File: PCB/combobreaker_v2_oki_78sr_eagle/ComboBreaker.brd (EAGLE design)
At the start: 52 x 44.5 mm, 9 parts, among them J1 7-35v

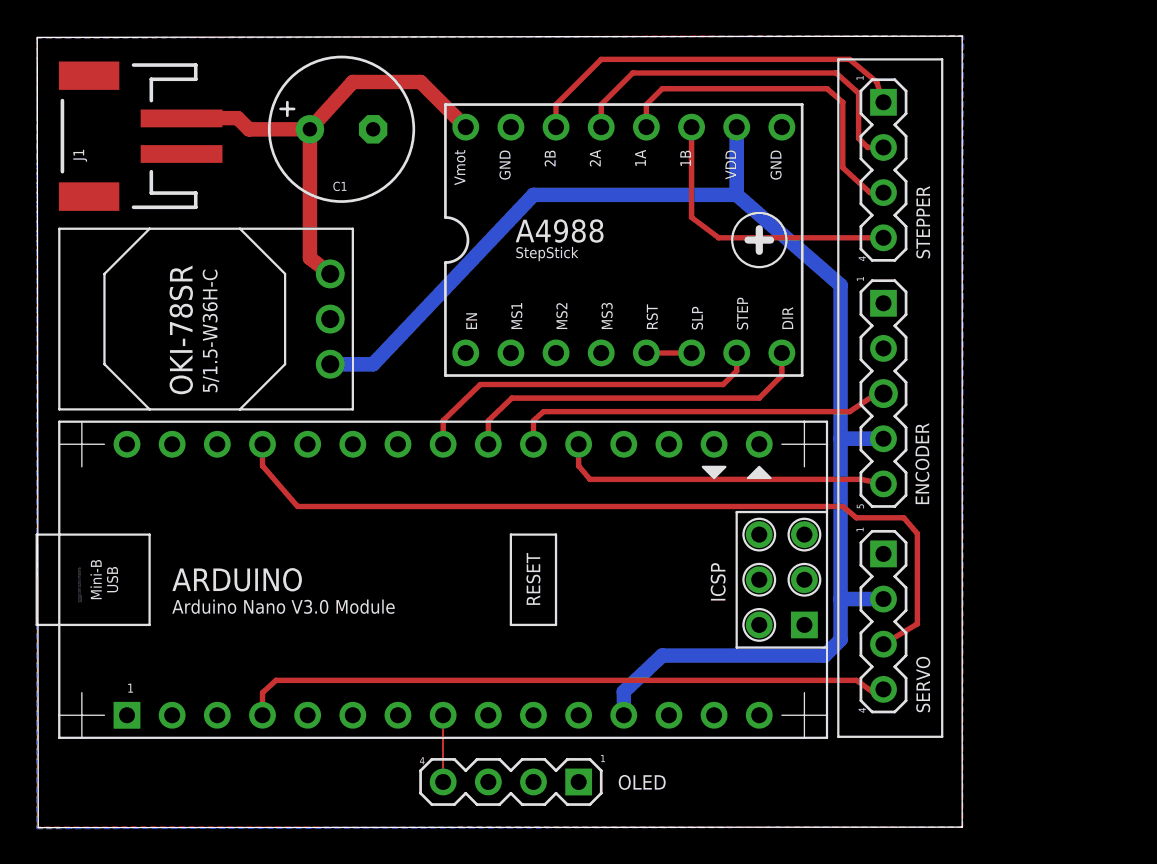
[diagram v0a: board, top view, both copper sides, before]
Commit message: Added I2C OLED Display
* Added I2C header pins for OLED display
* Reoriented JST power connector
* Rerouted VCC
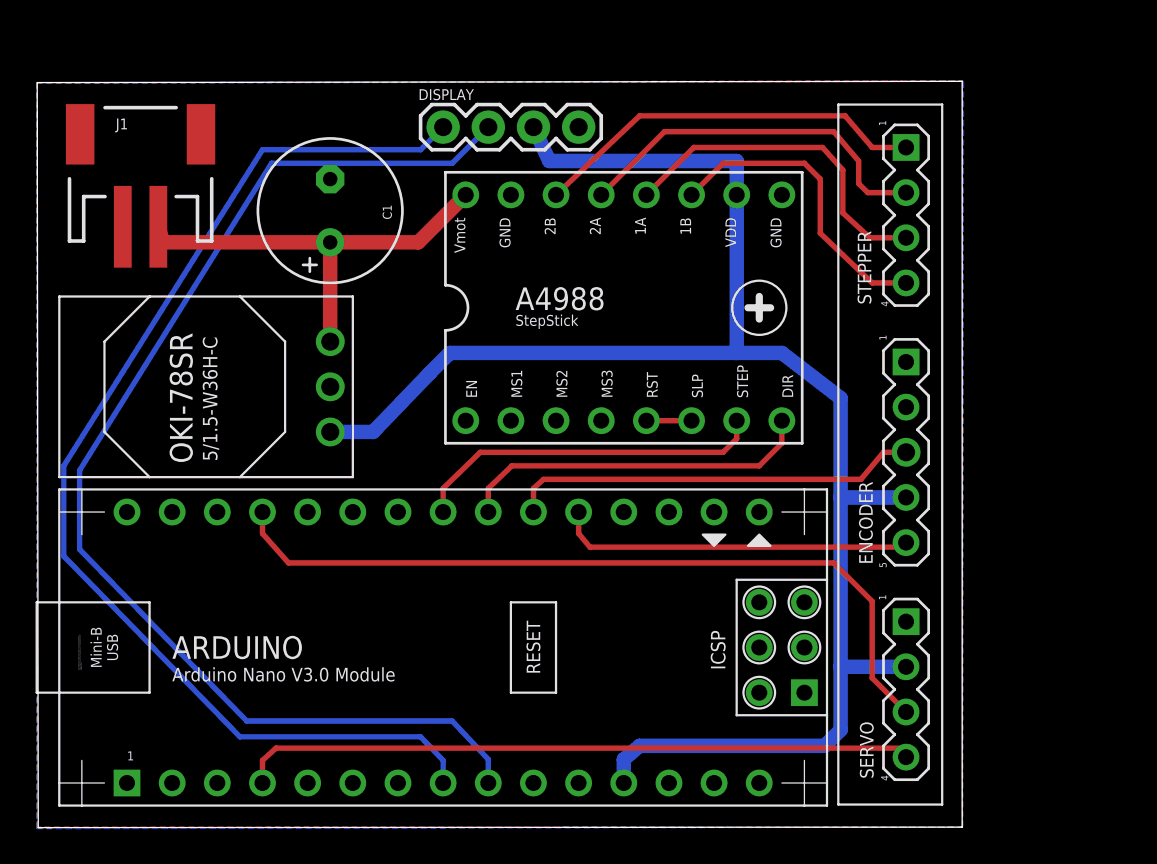
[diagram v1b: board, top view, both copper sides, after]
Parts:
- removed OLED: (no value), con-lstb:MA04-1
- added DISPLAY: OLED_I2C, SparkFun-Connectors:1X04
- moved C1 4.62 mm to (16.5, 34.7), turned to 90 degrees
- moved SERVO 4.02 mm to (48.9, 7.75)
- moved A4988 3.81 mm to (34.3, 29.2)
- moved ARDUINO 3.81 mm to (19.0, 10.1)
- moved OKI-78SR 3.81 mm to (6.35, 24.8)
- moved ENCODER 3.54 mm to (48.9, 21.1)
- moved STEPPER 2.84 mm to (48.9, 34.4)
- moved J1 1.98 mm to (5.84, 37.5), turned to 0 degrees
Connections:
- removed net N$4: OLED.2
- net +5V: now also DISPLAY.2
- net GND: now also DISPLAY.1; no longer OLED.1
- net SCL: now also DISPLAY.3; no longer OLED.3
- net SDA: now also DISPLAY.4; no longer OLED.4
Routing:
- net SCL: track 0.00 -> 67.2 mm
- net SDA: track 11.3 -> 64.2 mm
- net +5V: track 78.0 -> 95.1 mm
- net D9_SERVO: track 47.0 -> 44.2 mm
- net VCC: track 27.2 -> 24.6 mm
- net D3_CH_B_BROWN: track 21.5 -> 23.2 mm
- net D2_CH_A_WHITE: track 18.7 -> 20.2 mm
- net FEEDBACK: track 36.7 -> 38.0 mm
- net 1A_BLK: track 16.3 -> 17.3 mm
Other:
- board size 52 x 44.5 mm -> 52 x 42 mm

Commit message: Updated v2 Eagle PCB layout
* Added standoff holes
* Added descriptions
* Added mitre to board corners
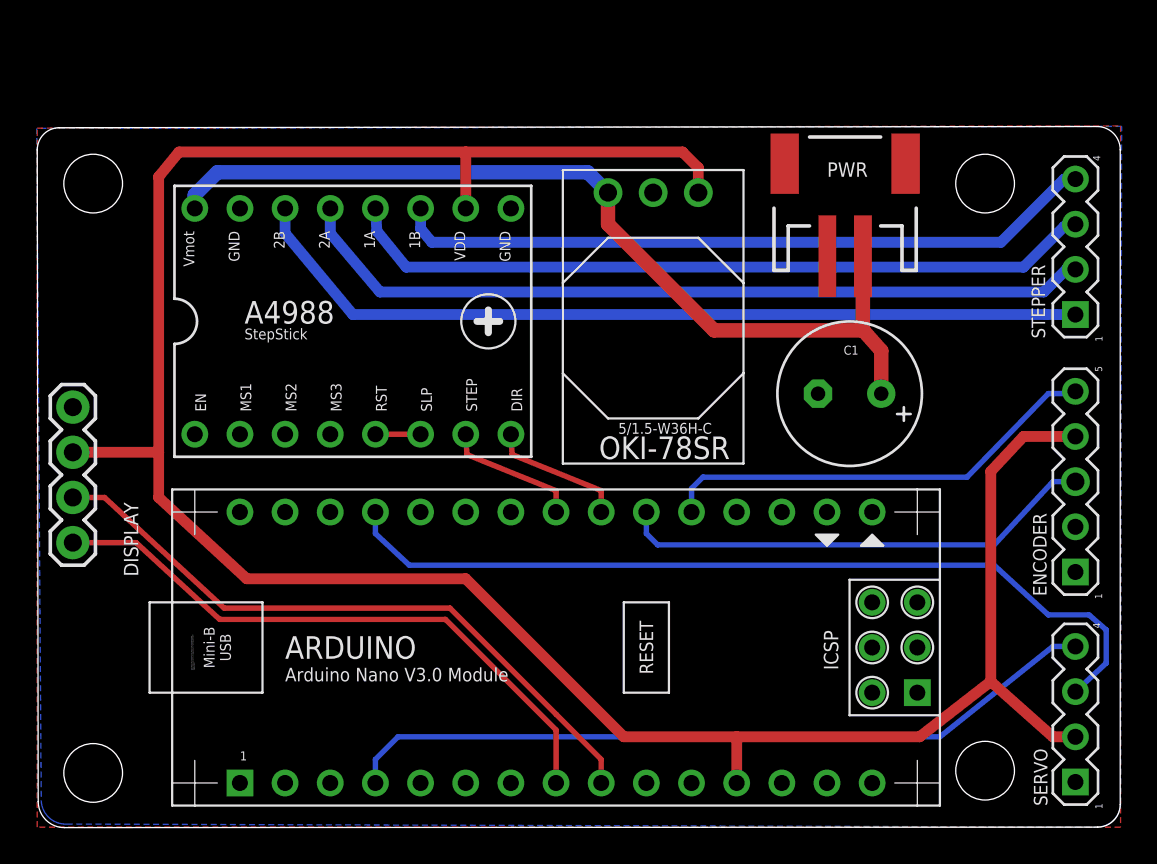
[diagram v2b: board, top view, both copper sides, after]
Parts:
- removed J1: 7-35v, SparkFun-Connectors:JST-2-SMD
- added PWR: 7-35v, SparkFun-Connectors:JST-2-SMD
- added U$1, U$2, U$3, U$4: (no value), SparkFun-Hardware:STAND-OFF
- DISPLAY: value OLED_I2C -> I2C
- moved DISPLAY 32.5 mm to (2.03, 23.6), turned to 270 degrees
- moved C1 31.0 mm to (45.7, 24.4), turned to 180 degrees
- moved OKI-78SR 28.3 mm to (34.7, 25.5), turned to 180 degrees
- moved A4988 15.3 mm to (19.1, 28.4)
- moved STEPPER 9.69 mm to (58.4, 32.6), turned to 90 degrees
- moved ENCODER 9.67 mm to (58.4, 19.4), turned to 90 degrees
- moved SERVO 9.63 mm to (58.4, 6.35), turned to 90 degrees
- moved ARDUINO 6.35 mm to (25.4, 10.1)
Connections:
- net GND: now also PWR.1; no longer J1.1
- net VCC: now also PWR.2; no longer J1.2
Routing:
- net +5V: track 95.1 -> 138.3 mm
- net SCL: track 67.2 -> 37.0 mm
- net SDA: track 64.2 -> 34.4 mm
- net VCC: track 24.6 -> 51.7 mm
- net 2B_BLU: track 22.3 -> 48.0 mm
- net 2A_RED: track 20.9 -> 45.4 mm
- net 1B_GRN: track 19.2 -> 42.5 mm
- net 1A_BLK: track 17.3 -> 39.8 mm
- net N$2: track 20.2 -> 7.75 mm
- net N$3: track 20.0 -> 7.75 mm
- net D2_CH_A_WHITE: track 20.2 -> 25.2 mm
- net FEEDBACK: track 38.0 -> 43.0 mm
- net D9_SERVO: track 44.2 -> 48.7 mm
- net D3_CH_B_BROWN: track 23.2 -> 27.2 mm
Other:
- board size 52 x 42 mm -> 60.9 x 39.4 mm
- board text added: "+5V"
- board text added: "GND"
- board text added: "SCL"
- board text added: "SDA"
- board text added: "VCC"
